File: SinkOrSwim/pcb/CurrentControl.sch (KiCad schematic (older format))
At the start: 7 parts

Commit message: First annotation
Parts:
- gave numbers to parts that had none: 7
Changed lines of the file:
@@
 $EndDescr
 $Comp
-L R R?
+L R R203
 U 1 1 54DC48BE
 P 7900 4200
-F 0 "R?" V 7980 4200 50  0000 C CNN
+F 0 "R203" V 7980 4200 50  0000 C CNN
 F 1 ".1" V 7907 4201 50  0000 C CNN
 F 2 "Resistors_SMD:R_2512_HandSoldering" V 7830 4200 30  0000 C CNN
@@
 $EndComp
 $Comp
-L R R?
+L R R201
 U 1 1 54DC48CB
 P 4200 4300
-F 0 "R?" V 4280 4300 50  0000 C CNN
+F 0 "R201" V 4280 4300 50  0000 C CNN
 F 1 "R" V 4207 4301 50  0000 C CNN
 F 2 "" V 4130 4300 30  0000 C CNN
@@
 	7900 4450 7900 5150
 $Comp
-L GND #PWR?
+L GND #PWR202
 U 1 1 54DC48D7
 P 5750 3550
-F 0 "#PWR?" H 5750 3300 60  0001 C CNN
+F 0 "#PWR202" H 5750 3300 60  0001 C CNN
 F 1 "GND" H 5750 3400 60  0000 C CNN
 F 2 "" H 5750 3550 60  0000 C CNN
@@
 Connection ~ 7900 5000
 $Comp
-L POT RV?
+L POT RV201
 U 1 1 54DC48F1
 P 4200 3450
-F 0 "RV?" H 4200 3350 50  0000 C CNN
+F 0 "RV201" H 4200 3350 50  0000 C CNN
 F 1 "POT" H 4200 3450 50  0000 C CNN
 F 2 "" H 4200 3450 60  0000 C CNN
@@
 	7900 1750 7900 2900
 $Comp
-L C C?
+L C C201
 U 1 1 54DC4901
 P 5100 2500
-F 0 "C?" H 5150 2600 50  0000 L CNN
+F 0 "C201" H 5150 2600 50  0000 L CNN
 F 1 "C" H 5150 2400 50  0000 L CNN
 F 2 "" H 5138 2350 30  0000 C CNN
@@
 Connection ~ 5100 2150
 $Comp
-L GND #PWR?
+L GND #PWR201
 U 1 1 54DC490A
 P 5100 2750
-F 0 "#PWR?" H 5100 2500 60  0001 C CNN
+F 0 "#PWR201" H 5100 2500 60  0001 C CNN
 F 1 "GND" H 5100 2600 60  0000 C CNN
 F 2 "" H 5100 2750 60  0000 C CNN
@@
 	5100 2750 5100 2700
 $Comp
-L LMV358 U?
+L LMV358 U201
 U 1 1 54DC4911
 P 5850 3100
-F 0 "U?" H 5800 3300 60  0000 L CNN
+F 0 "U201" H 5800 3300 60  0000 L CNN
 F 1 "LMV358" H 5800 2850 60  0000 L CNN
 F 2 "" H 5850 3100 60  0000 C CNN
@@
 $EndComp
 $Comp
-L BUK9575-100A Q?
+L BUK9575-100A Q201
 U 1 1 54DC4918
 P 7800 3100
-F 0 "Q?" H 7810 3270 50  0000 R CNN
+F 0 "Q201" H 7810 3270 50  0000 R CNN
 F 1 "BUK9575-100A" H 7750 2950 50  0000 R CNN
 F 2 "" H 7800 3100 60  0000 C CNN
@@
 	7900 1750 8350 1750
 $Comp
-L R R?
+L R R202
 U 1 1 54DC4D3B
 P 6950 3100
-F 0 "R?" V 7030 3100 50  0000 C CNN
+F 0 "R202" V 7030 3100 50  0000 C CNN
 F 1 "1K" V 6957 3101 50  0000 C CNN
 F 2 "" V 6880 3100 30  0000 C CNN

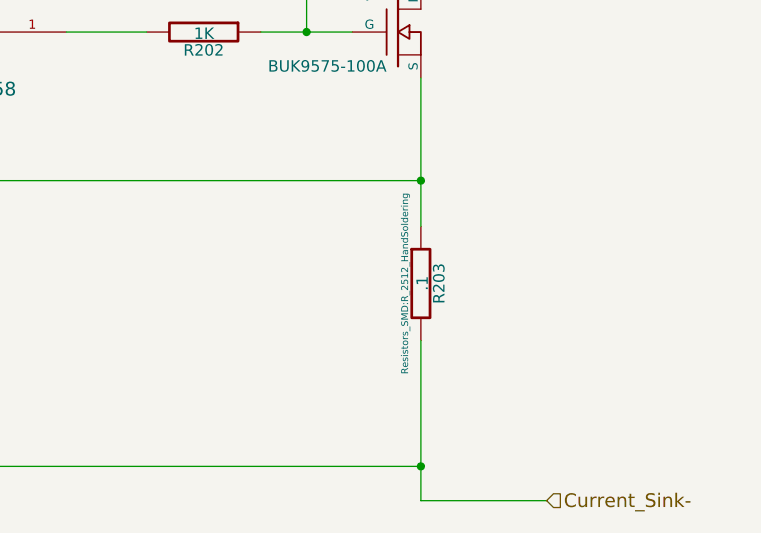
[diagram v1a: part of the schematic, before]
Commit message: Footprints associated and parts on pcb
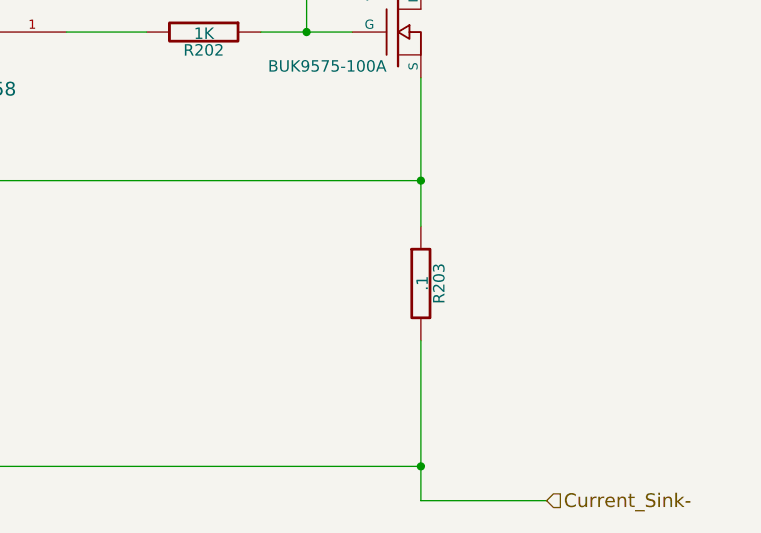
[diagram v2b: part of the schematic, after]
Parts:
- C201: footprint (none) -> Capacitors_SMD:C_0805_HandSoldering
- Q201: footprint (none) -> Transistors_TO-220:TO-220_FET-GDS_Vertical
- R201, R202: footprint (none) -> Resistors_SMD:R_0805_HandSoldering
- R203: footprint Resistors_SMD:R_2512_HandSoldering -> Resistors_ThroughHole:Resistor_Horizontal_RM15mm; MPN (none) -> Value
- RV201: footprint (none) -> pcb:Potiometer_Bourns_3362P; MPN (none) -> 3362P-1
- U201: footprint (none) -> SMD_Packages:SOIC-8-N; MPN (none) -> LMV358IDT
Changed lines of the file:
@@
 F 0 "R203" V 7980 4200 50  0000 C CNN
 F 1 ".1" V 7907 4201 50  0000 C CNN
-F 2 "Resistors_SMD:R_2512_HandSoldering" V 7830 4200 30  0000 C CNN
-F 3 "" H 7900 4200 30  0000 C CNN
+F 2 "Resistors_ThroughHole:Resistor_Horizontal_RM15mm" V 7830 4200 30  0001 C CNN
+F 3 "http://www.vishay.com/docs/28730/acseries.pdf" H 7900 4200 30  0001 C CNN
+F 4 "Value" H 7900 4200 60  0001 C CNN "MPN"
 	1    7900 4200
 	1    0    0    -1
@@
 F 0 "R201" V 4280 4300 50  0000 C CNN
 F 1 "R" V 4207 4301 50  0000 C CNN
-F 2 "" V 4130 4300 30  0000 C CNN
+F 2 "Resistors_SMD:R_0805_HandSoldering" V 4130 4300 30  0001 C CNN
 F 3 "" H 4200 4300 30  0000 C CNN
 	1    4200 4300
@@
 	7900 4450 7900 5150
 $Comp
-L GND #PWR202
+L GND #PWR03
 U 1 1 54DC48D7
 P 5750 3550
-F 0 "#PWR202" H 5750 3300 60  0001 C CNN
+F 0 "#PWR03" H 5750 3300 60  0001 C CNN
 F 1 "GND" H 5750 3400 60  0000 C CNN
 F 2 "" H 5750 3550 60  0000 C CNN
@@
 F 0 "RV201" H 4200 3350 50  0000 C CNN
 F 1 "POT" H 4200 3450 50  0000 C CNN
-F 2 "" H 4200 3450 60  0000 C CNN
-F 3 "" H 4200 3450 60  0000 C CNN
+F 2 "pcb:Potiometer_Bourns_3362P" H 4200 3450 60  0001 C CNN
+F 3 "http://www.bourns.com/data/global/pdfs/3362.pdf" H 4200 3450 60  0001 C CNN
+F 4 "3362P-1" H 4200 3450 60  0001 C CNN "MPN"
 	1    4200 3450
 	0    1    1    0
@@
 F 0 "C201" H 5150 2600 50  0000 L CNN
 F 1 "C" H 5150 2400 50  0000 L CNN
-F 2 "" H 5138 2350 30  0000 C CNN
+F 2 "Capacitors_SMD:C_0805_HandSoldering" H 5138 2350 30  0001 C CNN
 F 3 "" H 5100 2500 60  0000 C CNN
 	1    5100 2500
@@
 Connection ~ 5100 2150
 $Comp
-L GND #PWR201
+L GND #PWR04
 U 1 1 54DC490A
 P 5100 2750
-F 0 "#PWR201" H 5100 2500 60  0001 C CNN
+F 0 "#PWR04" H 5100 2500 60  0001 C CNN
 F 1 "GND" H 5100 2600 60  0000 C CNN
 F 2 "" H 5100 2750 60  0000 C CNN
@@
 F 0 "U201" H 5800 3300 60  0000 L CNN
 F 1 "LMV358" H 5800 2850 60  0000 L CNN
-F 2 "" H 5850 3100 60  0000 C CNN
-F 3 "" H 5850 3100 60  0000 C CNN
+F 2 "SMD_Packages:SOIC-8-N" H 5850 3100 60  0001 C CNN
+F 3 "http://www.st.com/web/en/resource/technical/document/datasheet/CD00079372.pdf" H 5850 3100 60  0001 C CNN
+F 4 "LMV358IDT" H 5850 3100 60  0001 C CNN "MPN"
 	1    5850 3100
 	1    0    0    -1
@@
 F 0 "Q201" H 7810 3270 50  0000 R CNN
 F 1 "BUK9575-100A" H 7750 2950 50  0000 R CNN
-F 2 "" H 7800 3100 60  0000 C CNN
+F 2 "Transistors_TO-220:TO-220_FET-GDS_Vertical" H 7800 3100 60  0001 C CNN
 F 3 "" H 7800 3100 60  0000 C CNN
 	1    7800 3100
@@
 F 0 "R202" V 7030 3100 50  0000 C CNN
 F 1 "1K" V 6957 3101 50  0000 C CNN
-F 2 "" V 6880 3100 30  0000 C CNN
+F 2 "Resistors_SMD:R_0805_HandSoldering" V 6880 3100 30  0001 C CNN
 F 3 "" H 6950 3100 30  0000 C CNN
 	1    6950 3100

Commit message: Fixed some drc items and started on heatsink footprint.
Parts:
- added P201: CONN_01X01, symbol CONN_01X01
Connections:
- no-connect marks 0 -> 2
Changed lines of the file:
@@
 	4350 2150 5750 2150
 Connection ~ 4350 2150
-Wire Wire Line
-	5750 2150 5750 2700
 Text Label 4650 2150 0    60   ~ 0
 2.7V
@@
 Text HLabel 8450 5150 2    60   Input ~ 0
 Current_Sink-
+$Comp
+L CONN_01X01 P201
+U 1 1 54E0DC1E
+P 8900 3400
+F 0 "P201" H 8900 3500 50  0000 C CNN
+F 1 "CONN_01X01" V 9000 3400 50  0000 C CNN
+F 2 "" H 8900 3400 60  0000 C CNN
+F 3 "" H 8900 3400 60  0000 C CNN
+	1    8900 3400
+	1    0    0    -1
+$EndComp
+NoConn ~ 4200 3200
+NoConn ~ 8700 3400
+Wire Wire Line
+	5750 2150 5750 2700
 $EndSCHEMATC

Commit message: Finished heatsink footprint and first stab at pcb layout.
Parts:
- P201: footprint (none) -> pcb:FA-T220-38E
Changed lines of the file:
@@
 F 0 "P201" H 8900 3500 50  0000 C CNN
 F 1 "CONN_01X01" V 9000 3400 50  0000 C CNN
-F 2 "" H 8900 3400 60  0000 C CNN
+F 2 "pcb:FA-T220-38E" H 8900 3400 60  0001 C CNN
 F 3 "" H 8900 3400 60  0000 C CNN
 	1    8900 3400

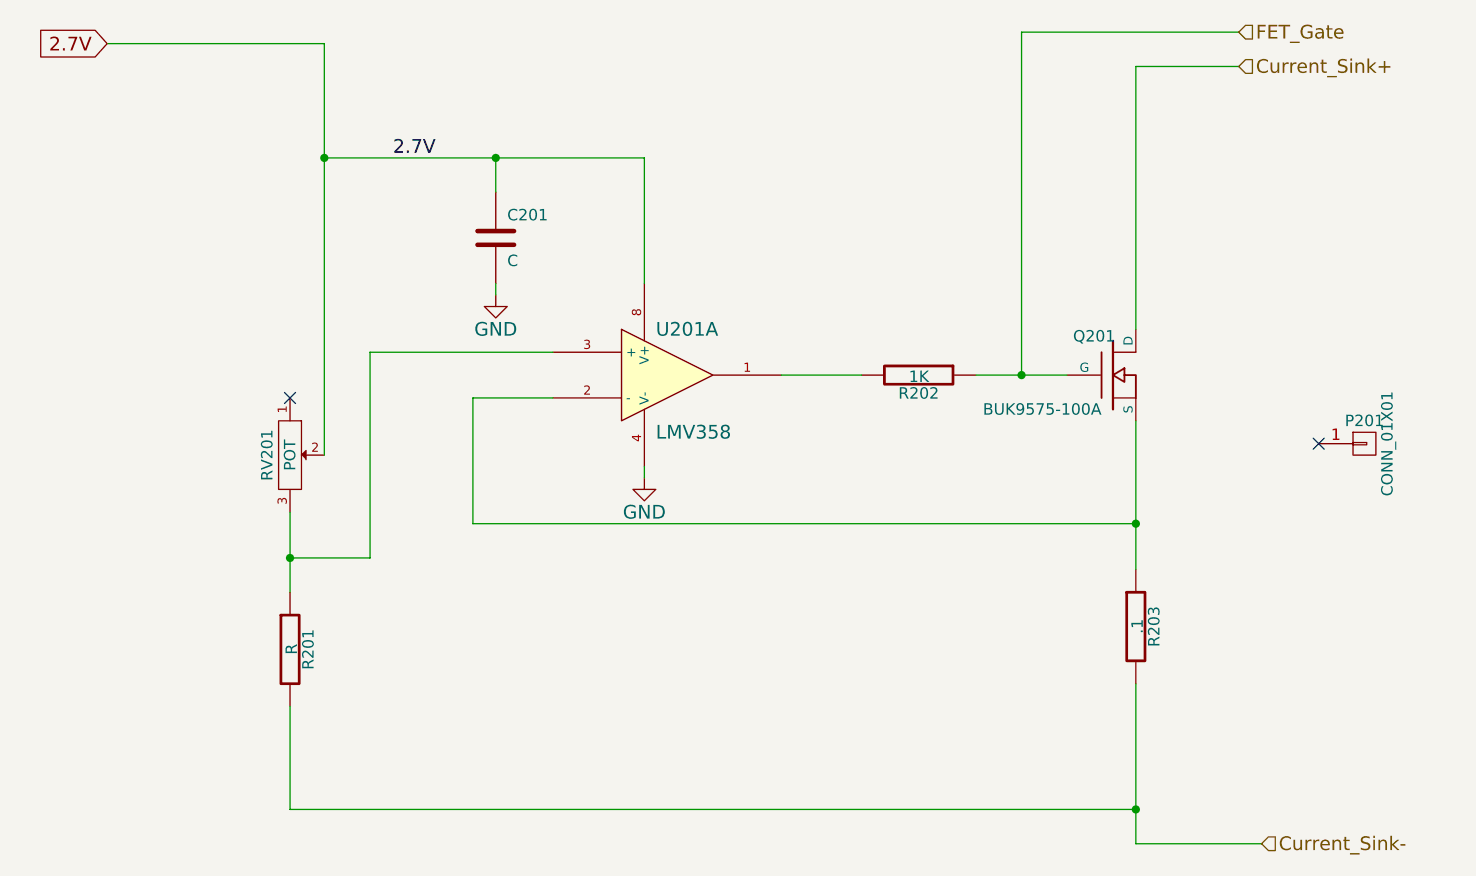
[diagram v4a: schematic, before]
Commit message: Find new terminal blocks.  Set resistor divider values.  Rearrange POT and fixed resistor.
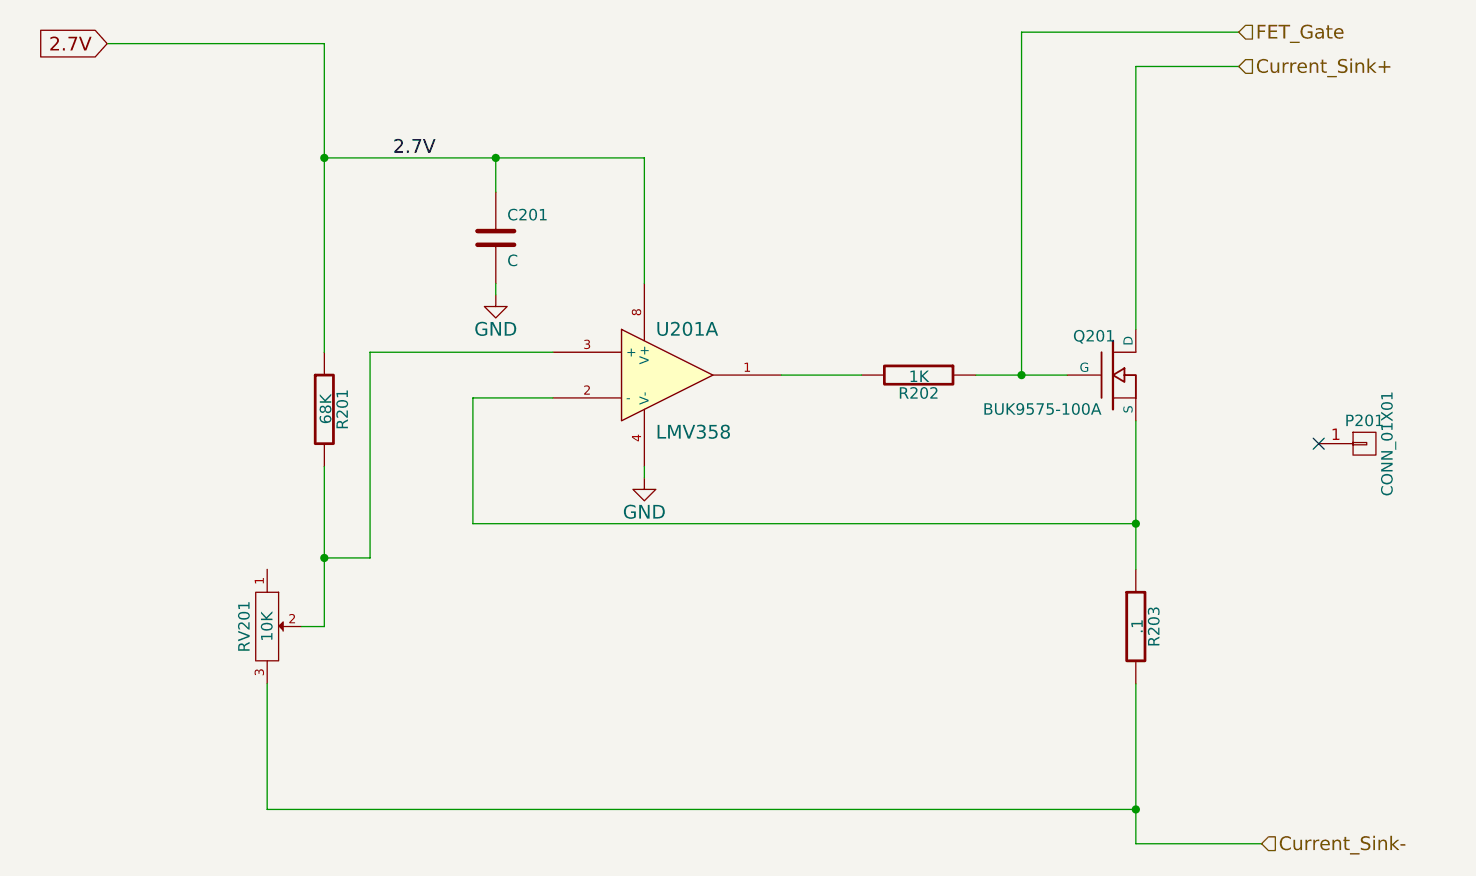
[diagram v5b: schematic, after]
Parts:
- R201: value R -> 68K; MPN (none) -> Value
- RV201: value POT -> 10K
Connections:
- net 2.7V: now also R201.1; no longer RV201.2
- net Current_Sink-: now also RV201.3; no longer R201.2
- new net: R201.2, RV201.2, U201.3 (+)
- no-connect marks 2 -> 1
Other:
- moved on the sheet: R201, RV201
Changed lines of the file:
@@
 L R R201
 U 1 1 54DC48CB
-P 4200 4300
-F 0 "R201" V 4280 4300 50  0000 C CNN
-F 1 "R" V 4207 4301 50  0000 C CNN
-F 2 "Resistors_SMD:R_0805_HandSoldering" V 4130 4300 30  0001 C CNN
-F 3 "" H 4200 4300 30  0000 C CNN
-	1    4200 4300
+P 4350 3250
+F 0 "R201" V 4430 3250 50  0000 C CNN
+F 1 "68K" V 4357 3251 50  0000 C CNN
+F 2 "Resistors_SMD:R_0805_HandSoldering" V 4280 3250 30  0001 C CNN
+F 3 "" H 4350 3250 30  0000 C CNN
+F 4 "Value" H 4350 3250 60  0001 C CNN "MPN"
+	1    4350 3250
 	1    0    0    -1
 $EndComp
@@
 Connection ~ 7900 3750
 Wire Wire Line
-	4200 3700 4200 4050
-Wire Wire Line
-	4200 3900 4550 3900
-Wire Wire Line
 	4550 3900 4550 3000
 Wire Wire Line
 	4550 3000 5350 3000
-Connection ~ 4200 3900
 Wire Wire Line
-	4200 4550 4200 5000
+	4100 4450 4100 5000
 Wire Wire Line
-	4200 5000 7900 5000
+	4100 5000 7900 5000
 Connection ~ 7900 5000
-$Comp
-L POT RV201
-U 1 1 54DC48F1
-P 4200 3450
-F 0 "RV201" H 4200 3350 50  0000 C CNN
-F 1 "POT" H 4200 3450 50  0000 C CNN
-F 2 "pcb:Potiometer_Bourns_3362P" H 4200 3450 60  0001 C CNN
-F 3 "http://www.bourns.com/data/global/pdfs/3362.pdf" H 4200 3450 60  0001 C CNN
-F 4 "3362P-1" H 4200 3450 60  0001 C CNN "MPN"
-	1    4200 3450
-	0    1    1    0
-$EndComp
 Wire Wire Line
 	4350 2150 5750 2150
@@
 	3400 1650 4350 1650
 Wire Wire Line
-	4350 1650 4350 3450
+	4350 1650 4350 3000
 Text HLabel 8350 1750 2    60   Input ~ 0
 Current_Sink+
@@
 	1    0    0    -1
 $EndComp
-NoConn ~ 4200 3200
 NoConn ~ 8700 3400
 Wire Wire Line
 	5750 2150 5750 2700
+Connection ~ 4350 3900
+Wire Wire Line
+	4350 3900 4550 3900
+$Comp
+L POT RV201
+U 1 1 54DC48F1
+P 4100 4200
+F 0 "RV201" H 4100 4100 50  0000 C CNN
+F 1 "10K" H 4100 4200 50  0000 C CNN
+F 2 "pcb:Potiometer_Bourns_3362P" H 4100 4200 60  0001 C CNN
+F 3 "http://www.bourns.com/data/global/pdfs/3362.pdf" H 4100 4200 60  0001 C CNN
+F 4 "3362P-1" H 4100 4200 60  0001 C CNN "MPN"
+	1    4100 4200
+	0    1    1    0
+$EndComp
+Wire Wire Line
+	4350 4200 4250 4200
+Wire Wire Line
+	4350 3500 4350 4200
 $EndSCHEMATC

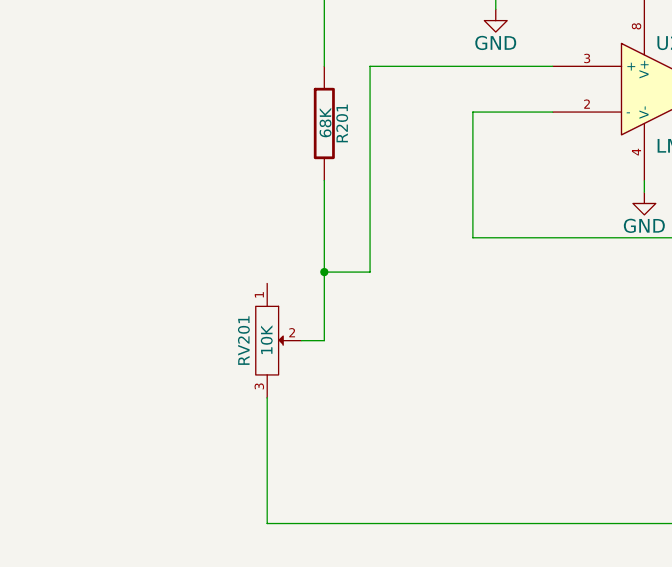
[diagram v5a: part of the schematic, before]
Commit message: Hide some of the labels on the pcb.  Moved the ground plane to the bottom.  More work reconnecting to do.
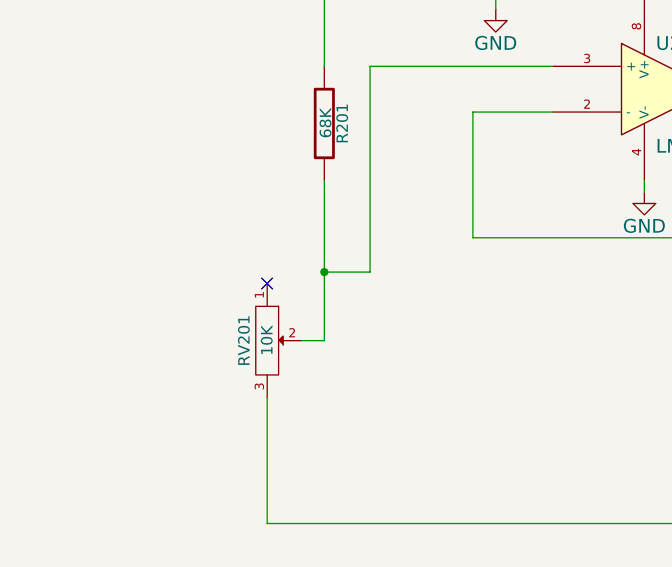
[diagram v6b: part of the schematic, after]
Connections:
- no-connect marks 1 -> 2
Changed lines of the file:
@@
 $EndComp
 NoConn ~ 8700 3400
-Wire Wire Line
-	5750 2150 5750 2700
 Connection ~ 4350 3900
 Wire Wire Line
@@
 Wire Wire Line
 	4350 3500 4350 4200
+Wire Wire Line
+	5750 2150 5750 2700
+NoConn ~ 4100 3950
 $EndSCHEMATC
